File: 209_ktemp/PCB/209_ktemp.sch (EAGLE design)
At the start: 9 parts

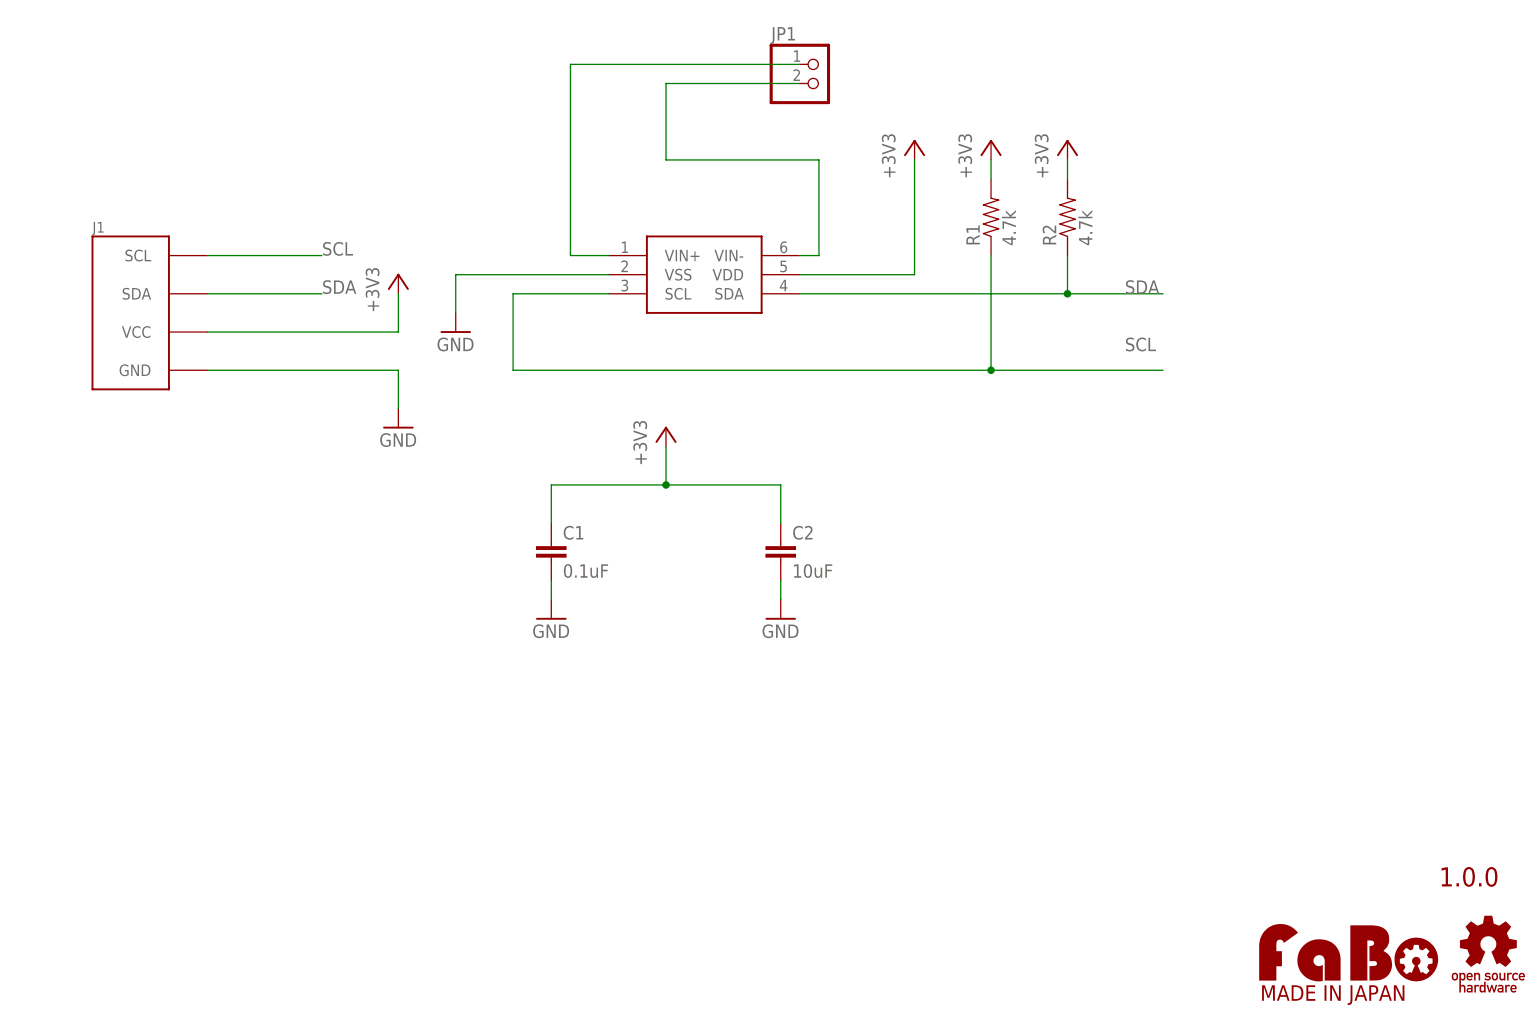
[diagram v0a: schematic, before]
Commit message: add product number
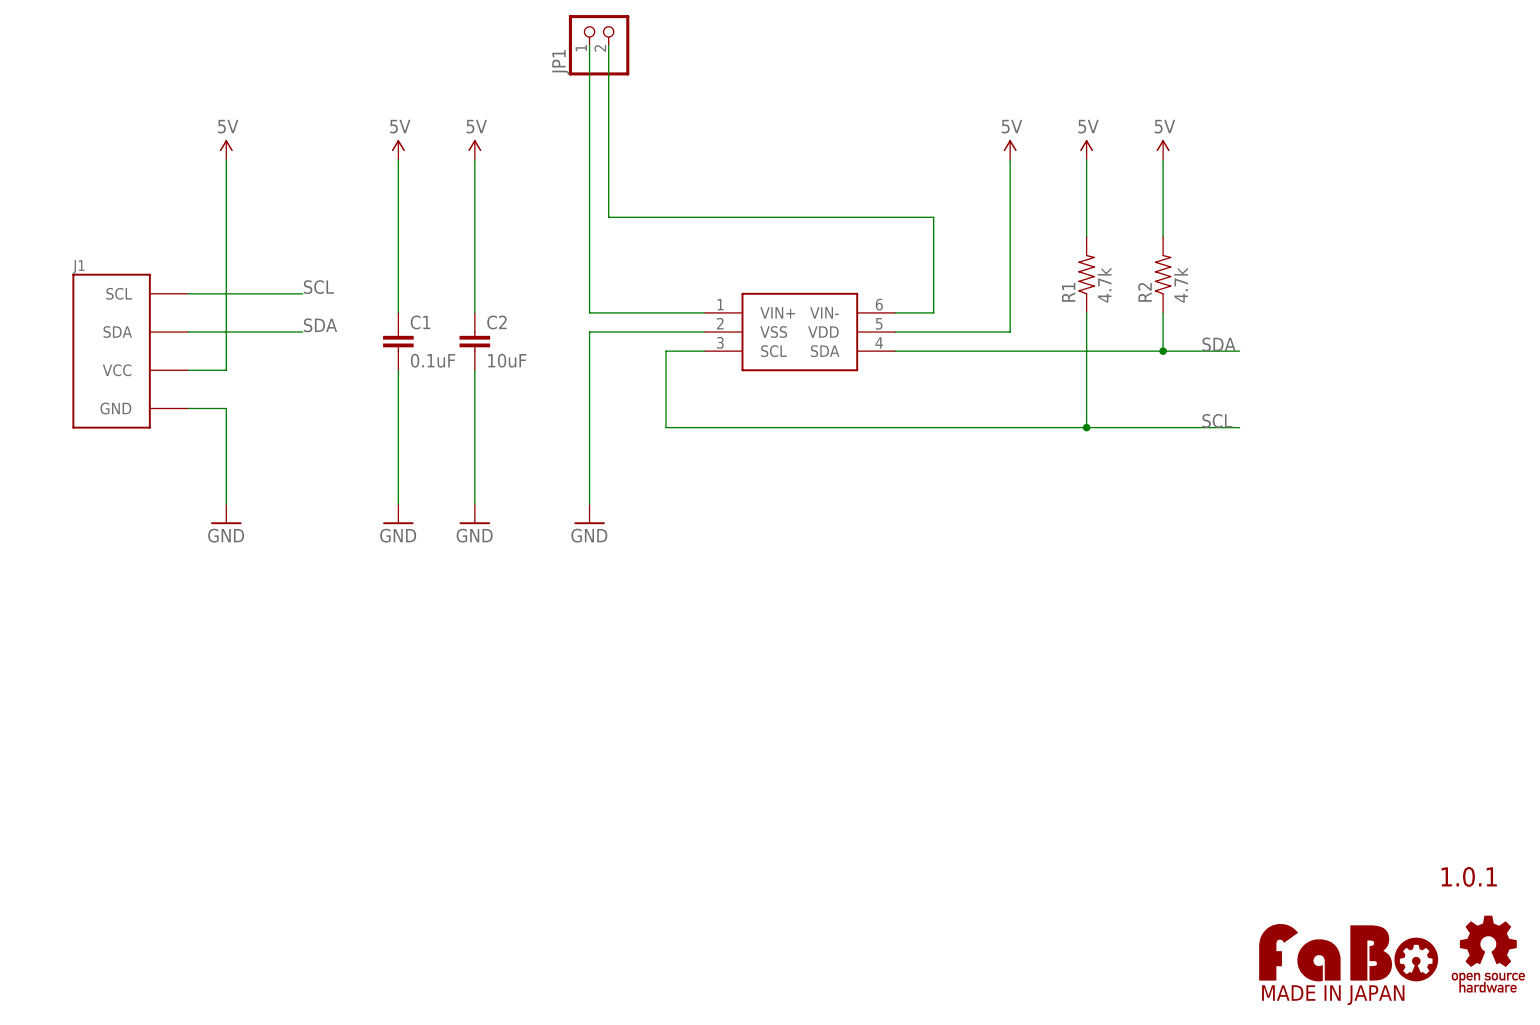
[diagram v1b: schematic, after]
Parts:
- J1: device gclue:BRICK_I2C -> FaBo-Template:FABO_BRICK_I2C
- U$3: device gclue:LOGO_OSHW_T-M -> FaBo-etc:LOGO_OSHW-T_M_BOTTOM
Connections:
- net +3V3 renamed 5V
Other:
- note added: "1.0.1"
- note removed: "1.0.0"
- moved on the sheet: C1, C2, J1, JP1, R1, R2

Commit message: change dru seeed
212 is draft
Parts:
- removed JP1: (no value), pinhead:PINHD-1X2
- removed R1, R2: 4.7k, gclue:RES-EIA0603
- added CN1: (no value), FaBo-PIN:PIN_HEADER_1X2
- C1, C2: device gclue:CAP-EIA0603 -> FaBo-Capacitor:CAPACITOR-0603
- U$3: device FaBo-etc:LOGO_OSHW-T_M_BOTTOM -> FaBo-etc:LOGO_OSHW-M_BOTTOM
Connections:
- removed net N$1: JP1.2, U$2.VIN-
- removed net N$3: JP1.1, U$2.VIN+
- new net VM: CN1.2, U$2.VIN-
- new net VP: CN1.1, U$2.VIN+
- net 5V: now also C1.2, C2.2; no longer C1.1, C2.1, R1.2, R2.2
- net GND: now also C1.1, C2.1; no longer C1.2, C2.2
- net SCL: no longer R1.1
- net SDA: no longer R2.1
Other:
- note added: "1.0.2"
- note removed: "1.0.1"
- moved on the sheet: C1, C2, J1

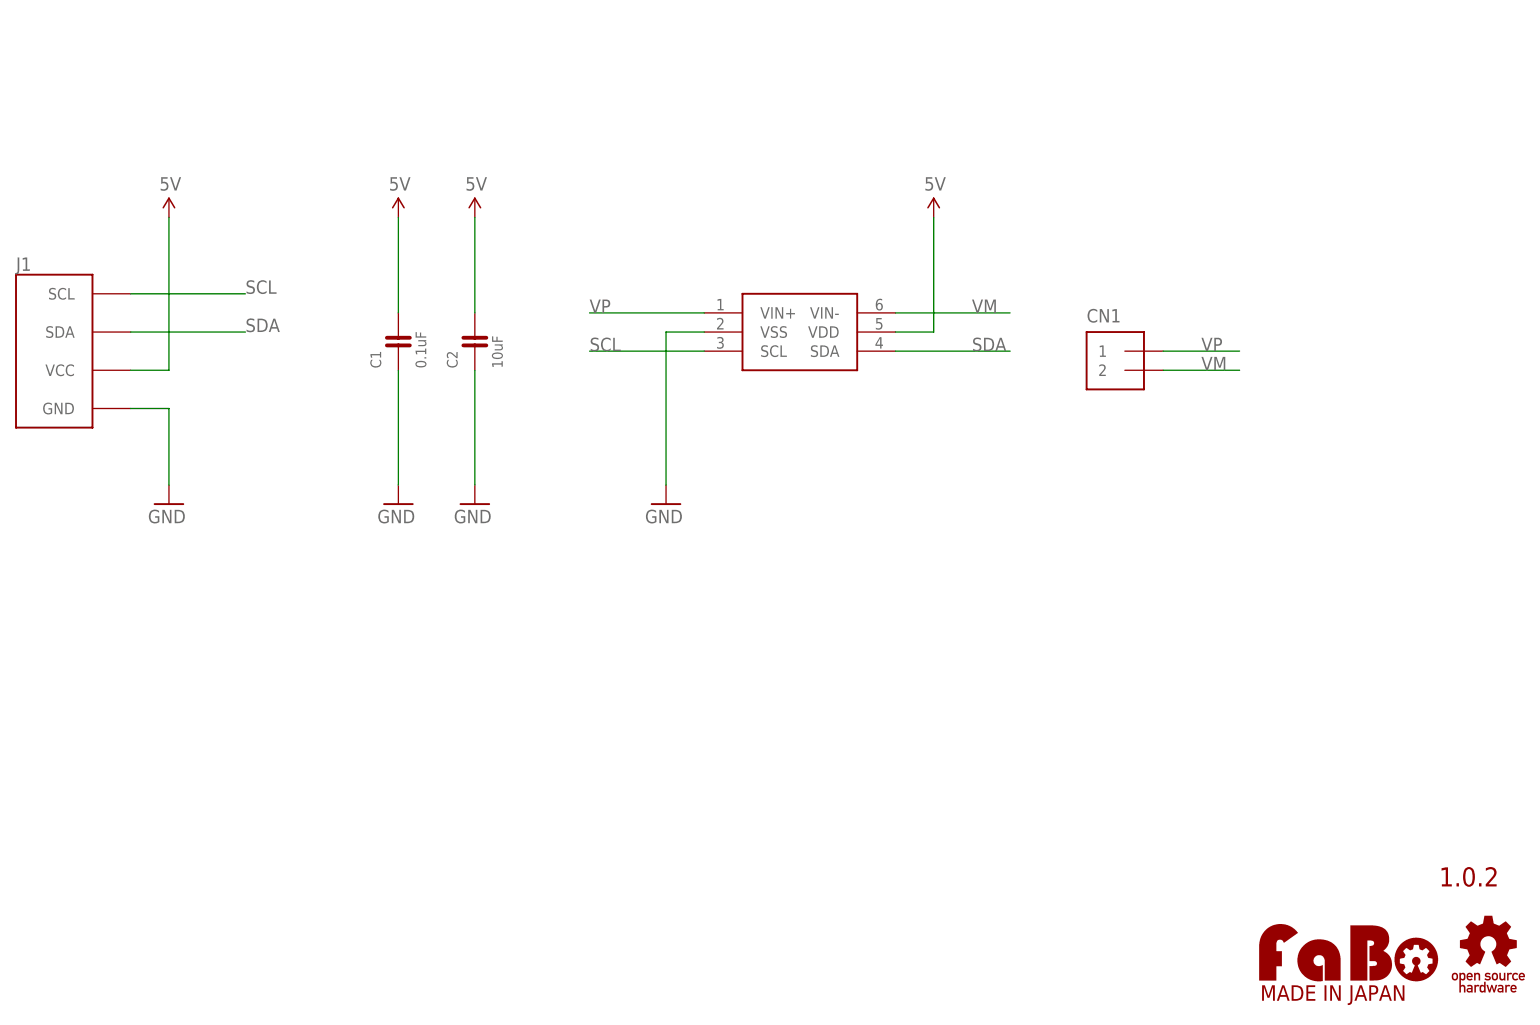
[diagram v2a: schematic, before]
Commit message: change 209 packages
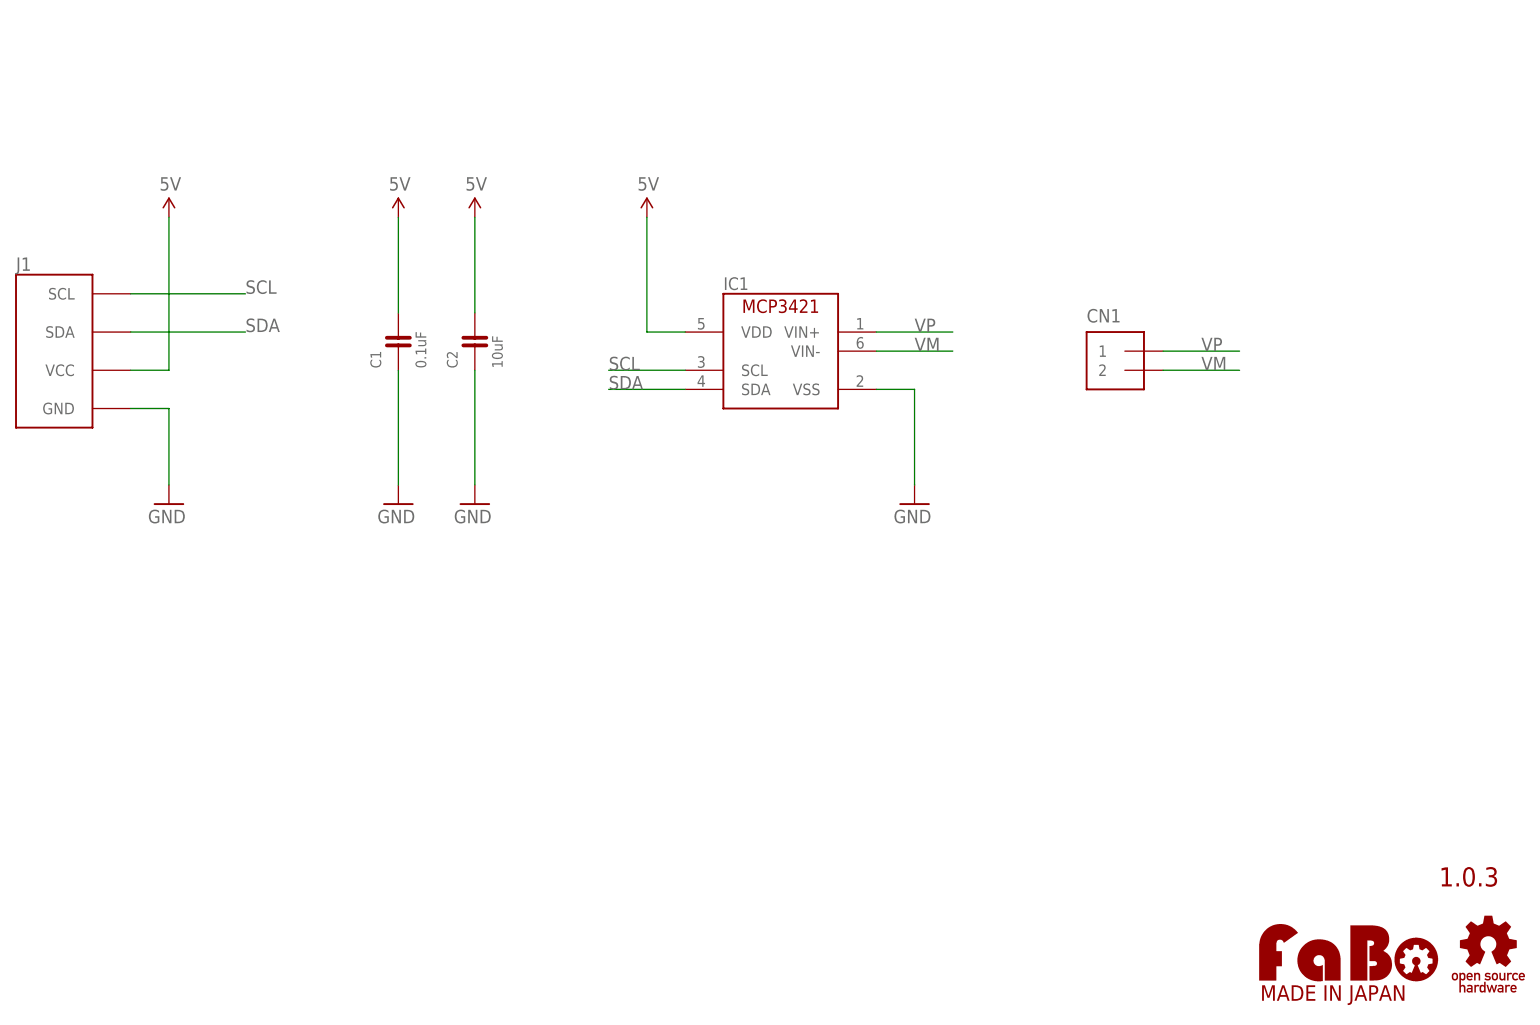
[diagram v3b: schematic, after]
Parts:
- removed U$2: MICROCHIP-MCP3421, gclueSensor:MICROCHIP-MCP3421
- added IC1: (no value), FaBo-Sensor:MCP3421
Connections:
- net 5V: now also IC1.VDD; no longer U$2.VDD
- net GND: now also IC1.VSS; no longer U$2.VSS
- net SCL: now also IC1.SCL; no longer U$2.SCL
- net SDA: now also IC1.SDA; no longer U$2.SDA
- net VM: now also IC1.VIN-; no longer U$2.VIN-
- net VP: now also IC1.VIN+; no longer U$2.VIN+
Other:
- note added: "1.0.3"
- note removed: "1.0.2"
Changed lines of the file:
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@@
 <setting verticaltext="up"/>
 </settings>
-<grid distance="0.1" unitdist="inch" unit="inch" style="lines" multiple="1" display="no" altdistance="0.01" altunitdist="inch" altunit="inch"/>
+<grid distance="0.1" unitdist="inch" unit="inch" style="lines" multiple="1" display="yes" altdistance="0.01" altunitdist="inch" altunit="inch"/>
 <layers>
 <layer number="1" name="Top" color="4" fill="1" visible="no" active="no"/>
@@
 </classes>
 <parts>
-<part name="U$2" library="gclueSensor" deviceset="MICROCHIP-MCP3421" device=""/>
 <part name="J1" library="FaBo-Template" deviceset="FABO_BRICK_I2C" device=""/>
 <part name="U$1" library="FaBo-etc" deviceset="A4L-LOC" device=""/>
@@
 <part name="CN1" library="FaBo-PIN" deviceset="PIN_HEADER_1X2" device=""/>
 <part name="U$3" library="FaBo-etc" deviceset="LOGO_OSHW" device="-M_BOTTOM"/>
+<part name="IC1" library="FaBo-Sensor" deviceset="MCP3421" device=""/>
 </parts>
 <sheets>
 <sheet>
 <plain>
-<text x="246.38" y="20.32" size="2.54" layer="94" align="bottom-center">1.0.2</text>
+<text x="246.38" y="20.32" size="2.54" layer="94" align="bottom-center">1.0.3</text>
 </plain>
 <instances>
-<instance part="U$2" gate="G$1" x="157.48" y="93.98"/>
 <instance part="J1" gate="G$1" x="60.96" y="91.44"/>
 <instance part="U$1" gate="G$1" x="0" y="0"/>
@@
 <instance part="GND2" gate="G$1" x="104.14" y="73.66"/>
 <instance part="GND3" gate="G$1" x="114.3" y="73.66"/>
-<instance part="GND4" gate="G$1" x="139.7" y="73.66"/>
+<instance part="GND4" gate="G$1" x="172.72" y="73.66"/>
 <instance part="5V1" gate="G$1" x="73.66" y="109.22"/>
 <instance part="5V2" gate="G$1" x="104.14" y="109.22"/>
 <instance part="5V3" gate="G$1" x="114.3" y="109.22"/>
-<instance part="5V4" gate="G$1" x="175.26" y="109.22"/>
+<instance part="5V4" gate="G$1" x="137.16" y="109.22"/>
 <instance part="C1" gate="G$1" x="104.14" y="91.44" rot="R90"/>
 <instance part="C2" gate="G$1" x="114.3" y="91.44" rot="R90"/>
 <instance part="CN1" gate="G$1" x="200.66" y="88.9" rot="R270"/>
 <instance part="U$3" gate="G$1" x="248.92" y="12.7"/>
+<instance part="IC1" gate="G$1" x="154.94" y="91.44"/>
 </instances>
 <busses>
@@
 <net name="SCL" class="0">
 <segment>
-<pinref part="U$2" gate="G$1" pin="SCL"/>
-<wire x1="144.78" y1="91.44" x2="129.54" y2="91.44" width="0.1524" layer="91"/>
-<label x="129.54" y="91.44" size="1.778" layer="95"/>
-</segment>
-<segment>
 <wire x1="68.58" y1="99.06" x2="83.82" y2="99.06" width="0.1524" layer="91"/>
 <label x="83.82" y="99.06" size="1.778" layer="95"/>
 <pinref part="J1" gate="G$1" pin="SCL"/>
 </segment>
+<segment>
+<pinref part="IC1" gate="G$1" pin="SCL"/>
+<wire x1="132.08" y1="88.9" x2="142.24" y2="88.9" width="0.1524" layer="91"/>
+<label x="132.08" y="88.9" size="1.778" layer="95"/>
+</segment>
 </net>
 <net name="SDA" class="0">
-<segment>
-<pinref part="U$2" gate="G$1" pin="SDA"/>
-<wire x1="170.18" y1="91.44" x2="185.42" y2="91.44" width="0.1524" layer="91"/>
-<label x="180.34" y="91.44" size="1.778" layer="95"/>
-</segment>
 <segment>
 <wire x1="68.58" y1="93.98" x2="83.82" y2="93.98" width="0.1524" layer="91"/>
@@
 <pinref part="J1" gate="G$1" pin="SDA"/>
 </segment>
+<segment>
+<pinref part="IC1" gate="G$1" pin="SDA"/>
+<wire x1="132.08" y1="86.36" x2="142.24" y2="86.36" width="0.1524" layer="91"/>
+<label x="132.08" y="86.36" size="1.778" layer="95"/>
+</segment>
 </net>
 <net name="VP" class="0">
-<segment>
-<pinref part="U$2" gate="G$1" pin="VIN+"/>
-<wire x1="144.78" y1="96.52" x2="129.54" y2="96.52" width="0.1524" layer="91"/>
-<label x="129.54" y="96.52" size="1.778" layer="95"/>
-</segment>
 <segment>
 <pinref part="CN1" gate="G$1" pin="1"/>
@@
 <label x="210.82" y="91.44" size="1.778" layer="95"/>
 </segment>
+<segment>
+<pinref part="IC1" gate="G$1" pin="VIN+"/>
+<wire x1="177.8" y1="93.98" x2="167.64" y2="93.98" width="0.1524" layer="91"/>
+<label x="172.72" y="93.98" size="1.778" layer="95"/>
+</segment>
 </net>
 <net name="VM" class="0">
-<segment>
-<pinref part="U$2" gate="G$1" pin="VIN-"/>
-<wire x1="185.42" y1="96.52" x2="170.18" y2="96.52" width="0.1524" layer="91"/>
-<label x="180.34" y="96.52" size="1.778" layer="95"/>
-</segment>
 <segment>
 <pinref part="CN1" gate="G$1" pin="2"/>
 <wire x1="215.9" y1="88.9" x2="205.74" y2="88.9" width="0.1524" layer="91"/>
 <label x="210.82" y="88.9" size="1.778" layer="95"/>
+</segment>
+<segment>
+<pinref part="IC1" gate="G$1" pin="VIN-"/>
+<wire x1="177.8" y1="91.44" x2="167.64" y2="91.44" width="0.1524" layer="91"/>
+<label x="172.72" y="91.44" size="1.778" layer="95"/>
 </segment>
 </net>
@@
 </segment>
 <segment>
-<pinref part="U$2" gate="G$1" pin="VSS"/>
-<wire x1="144.78" y1="93.98" x2="139.7" y2="93.98" width="0.1524" layer="91"/>
-<wire x1="139.7" y1="93.98" x2="139.7" y2="73.66" width="0.1524" layer="91"/>
+<pinref part="IC1" gate="G$1" pin="VSS"/>
 <pinref part="GND4" gate="G$1" pin="GND"/>
+<wire x1="167.64" y1="86.36" x2="172.72" y2="86.36" width="0.1524" layer="91"/>
+<wire x1="172.72" y1="86.36" x2="172.72" y2="73.66" width="0.1524" layer="91"/>
 </segment>
 </net>
@@
 </segment>
 <segment>
-<pinref part="U$2" gate="G$1" pin="VDD"/>
-<wire x1="170.18" y1="93.98" x2="175.26" y2="93.98" width="0.1524" layer="91"/>
-<wire x1="175.26" y1="93.98" x2="175.26" y2="109.22" width="0.1524" layer="91"/>
 <pinref part="5V4" gate="G$1" pin="5V"/>
-</segment>
-</net>
+<wire x1="137.16" y1="109.22" x2="137.16" y2="93.98" width="0.1524" layer="91"/>
+<pinref part="IC1" gate="G$1" pin="VDD"/>
+<wire x1="137.16" y1="93.98" x2="142.24" y2="93.98" width="0.1524" layer="91"/>
+</segment>
+</net>
